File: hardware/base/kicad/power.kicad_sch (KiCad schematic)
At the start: 49 parts, among them J1 24 V, J2 USB micro-B, Q11 AO3401A, U1 TPS54360BDDAR, U2 TPD4E05U06DQAR, U3 TPS62A02ADRLR

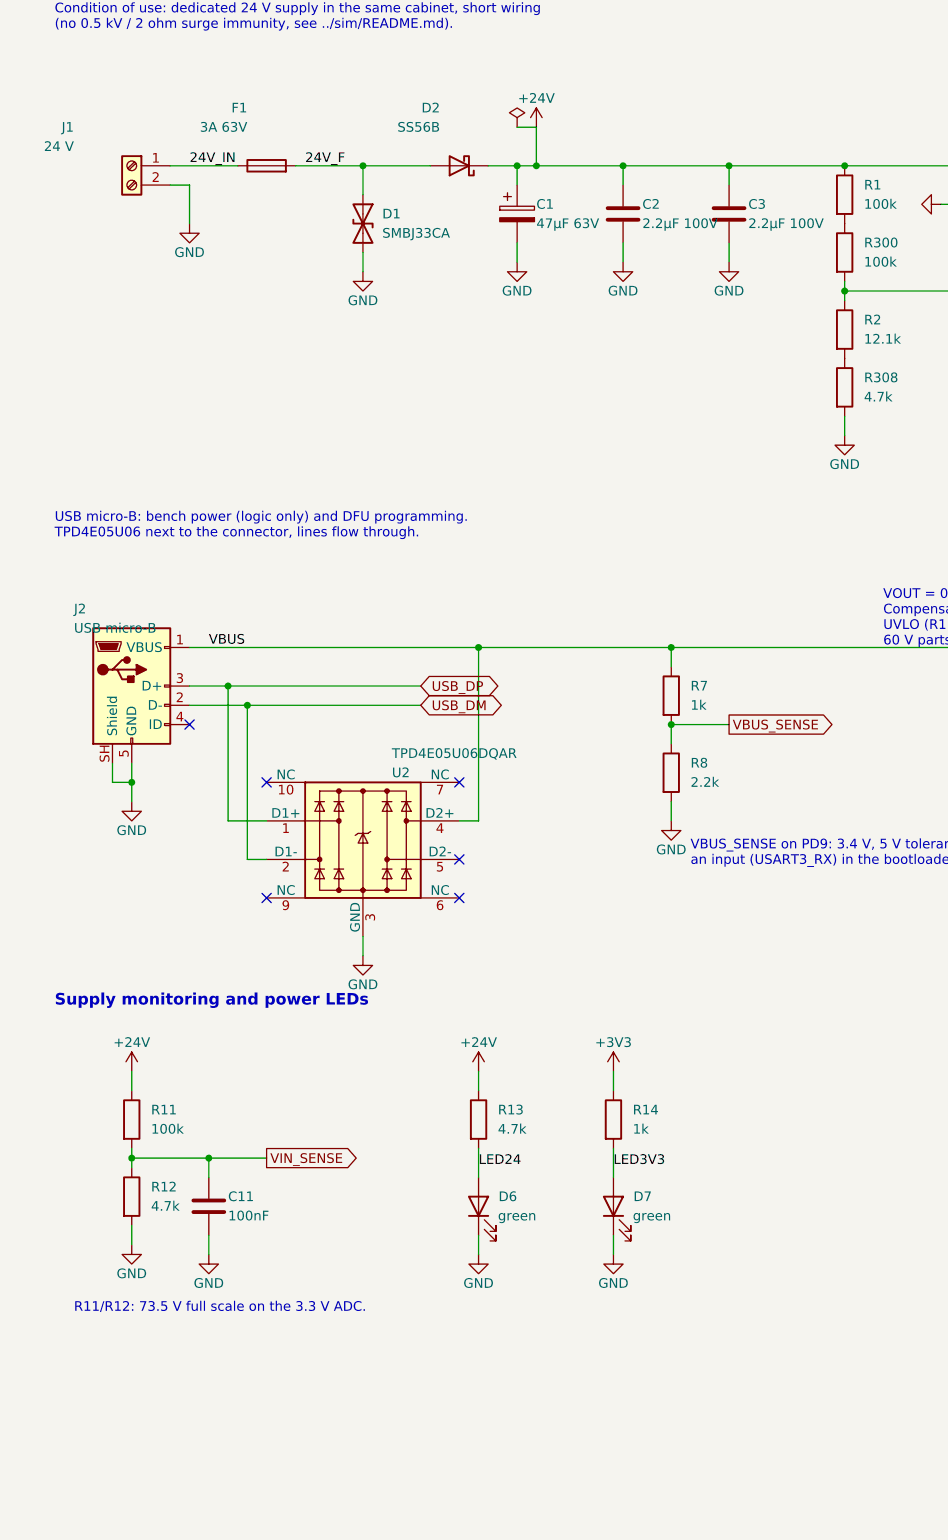
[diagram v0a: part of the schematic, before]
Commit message: Harden the base board protections and unify its terminal blocks
- TVS (SMBJ33CA) on the spindle EN and DIR drains: a relay coil driven
  without a flyback diode no longer avalanches the FET.
- ESD (5 x TPD4E05U06) on every signal of the local bus header.
- A single terminal block type, KF2EDGR-3.81-4P, five times. Pinout rule:
  pole 1 withstands 24 V, pole 2 is 0 V, so the power plug damages
  nothing whichever header it lands in.
- Functional earth on pole 3 of the power terminal block, replacing the
  M3 earth lug.
- 100 k pull-down on the DAC node: the 0-10 V output stays at 0 V while
  the DAC pin is not configured (reset, bootloader).
- "24V OUT" LED on +24V_DRV and test points on the four rails.
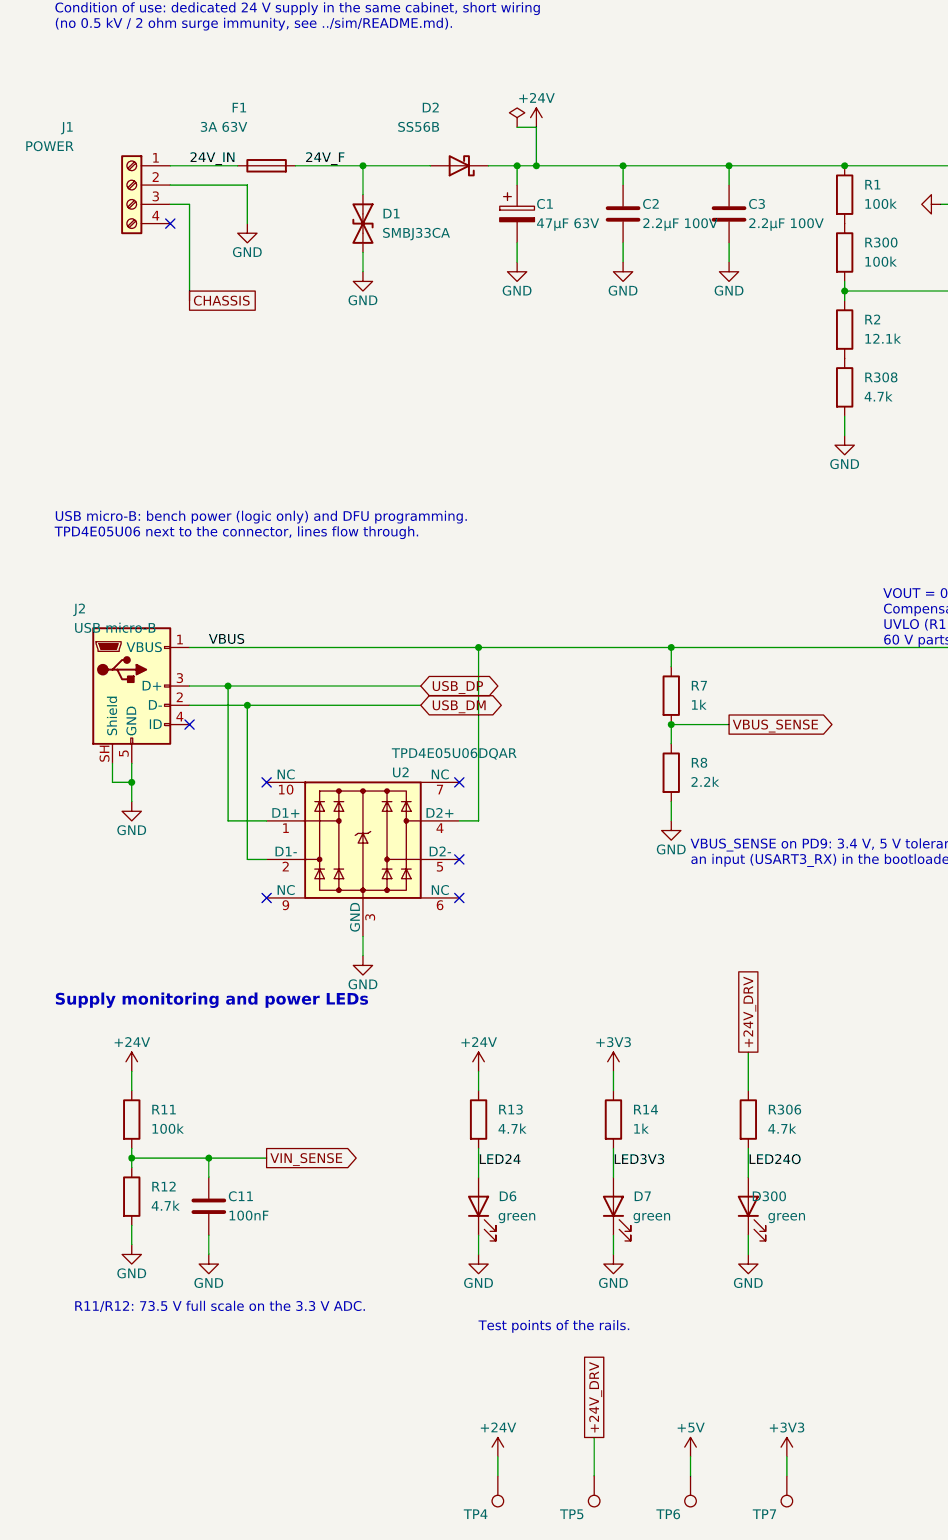
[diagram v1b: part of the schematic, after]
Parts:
- added D300: green, LED_SMD:LED_0603_1608Metric, symbol Device:LED
- added R306: 4.7k, Resistor_SMD:R_1206_3216Metric, symbol Device:R
- added TP4: +24V, TestPoint:TestPoint_Pad_D1.5mm, symbol Connector:TestPoint
- added TP5: +24V_DRV, TestPoint:TestPoint_Pad_D1.5mm, symbol Connector:TestPoint
- added TP6: +5V, TestPoint:TestPoint_Pad_D1.5mm, symbol Connector:TestPoint
- added TP7: +3V3, TestPoint:TestPoint_Pad_D1.5mm, symbol Connector:TestPoint
- J1: value 24 V -> POWER; footprint Connector_Phoenix_MSTB:PhoenixContact_MSTBA_2,5_2-G-5,08_1x02_P5.08mm_Horizontal -> Connector_Phoenix_MC:PhoenixContact_MC_1,5_4-G-3.81_1x04_P3.81mm_Horizontal; symbol Connector:Screw_Terminal_01x02 -> Connector:Screw_Terminal_01x04; LCSC C441204 -> C441184
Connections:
- net +24V: now also TP4.1
- net +3V3: now also TP7.1
- net +5V: now also TP6.1
- net GND: now also D300.1 (K)
- new net +24V_DRV: R306.1, TP5.1
- new net CHASSIS: J1.3 (Pin_3)
- new net LED24O: D300.2 (A), R306.2
- no-connect marks 7 -> 8
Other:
- note added: "Test points of the rails."

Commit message: Accept a 12 V or 24 V supply on the base board (10.8 to 30 V)
- Supply nets renamed +VIN and +VIN_OUT (silkscreen VIN OUT).
- UVLO 200 k over 47 k // 100 k: start 8.47 V (9.48 V worst case),
  stop 7.79 V; fuse 3.5 A (12H1350C).
- 0-10 V: OPA2990 rail-to-rail op amp supplied by +VIN, SS8550 current
  limit across the 120 ohm; 10 V into 10 k from 10.9 V of supply.
- E-stop and probe inputs: 2 x 4.7 k in parallel, shunts 1 k and 4.7 k.
- Buck simulated from 7.8 to 30 V with the smallest slope compensation
  the datasheet allows: 79 deg, 11.6 dB minimum.
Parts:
- F1: value 3A 63V -> 3.5A 63V; LCSC C182445 -> C182975
- R2: value 12.1k -> 47k; LCSC C25852 -> C25792
- R308: value 4.7k -> 100k; LCSC C25900 -> C25741
- TP4: value +24V -> +VIN
- TP5: value +24V_DRV -> +VIN_OUT
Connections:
- net EN: now also R308.1
- net GND: now also R2.2
- net +24V renamed +VIN
- net +24V_DRV renamed +VIN_OUT
- net 24V_F renamed VIN_F
- net 24V_IN renamed VIN_RAW
- net LED24 renamed LEDVIN
- net LED24O renamed LEDVOUT
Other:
- note added: "Logic supply VIN: 12 V or 24 V, 10.8 to 30 V (24 V: IEC 61131-2, 19.2 to 30 V). Fuse, bidirectional TVS, reverse polarity diode. Condition of use: dedicated supply in the same cabinet, short wiring (no 0.5 kV / 2 ohm surge immunity, see ../sim/README.md)."
- note added: "VOUT = 0.8 V x (1 + (R4 + R302)/(R5 + R303)) = 5.10 V, above VBUS; fsw = 658 kHz (R3 + R301 = 147 k). Compensation R6, C7 taken from the passive palette, simulated (sim/README.md). UVLO (R1 + R300 = 200 k, R2 // R308 = 32.0 k): start 8.47 V (9.48 V worst case), stop 7.79 V. 60 V parts throughout: the TVS clamps at 53.3 V."
- note removed: "24 V logic supply (IEC 61131-2: 19.2 to 30 V). Fuse, bidirectional TVS, reverse polarity diode. Condition of use: dedicated 24 V supply in the same cabinet, short wiring (no 0.5 kV / 2 ohm surge immunity, see ../sim/README.md)."
- note removed: "VOUT = 0.8 V x (1 + (R4 + R302)/(R5 + R303)) = 5.10 V, above VBUS; fsw = 658 kHz (R3 + R301 = 147 k). Compensation R6, C7 taken from the passive palette, simulated (sim/README.md). UVLO (R1 + R300 = 200 k, R2 + R308 = 16.8 k): start 15.25 V (16.97 V worst case), stop 14.57 V. 60 V parts throughout: the TVS clamps at 53.3 V."
- title: 24 V input, 5 V and 3.3 V bucks, USB -> 12 or 24 V input, 5 V and 3.3 V bucks, USB
- moved on the sheet: R308
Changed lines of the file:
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@@
 	(paper "A3")
 	(title_block
-		(title "24 V input, 5 V and 3.3 V bucks, USB")
+		(title "12 or 24 V input, 5 V and 3.3 V bucks, USB")
 		(date "2026-10-18")
 		(rev "A")

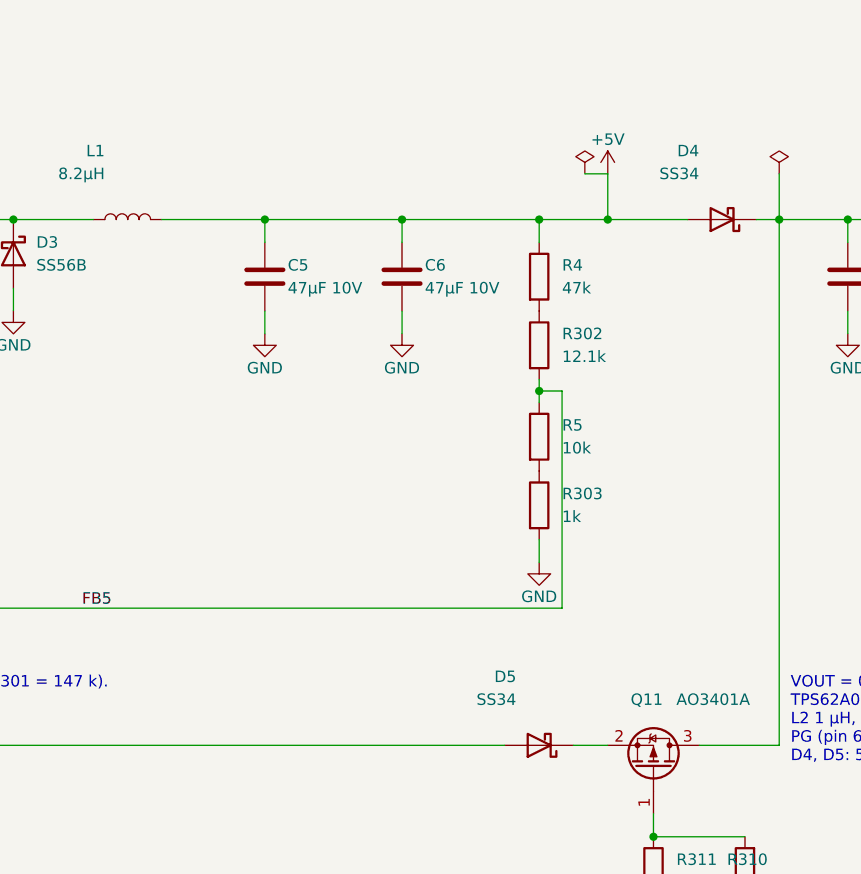
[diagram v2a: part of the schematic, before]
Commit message: Trim the base board BOM: 60 to 58 lines
- ESD of NRST and of the PWM output on one channel of the TPD4E05U06
  already used on the PHY lines, instead of a PESD5V0S1BA.
- SS56B instead of SS34 for the 5 V / USB OR-ing and the encoder
  supplies.
- One 100 uF 10 V X5R 1210 on the 5 V buck output instead of two 47 uF:
  about 55 uF at 5 V, inside the simulated 34-80 uF.
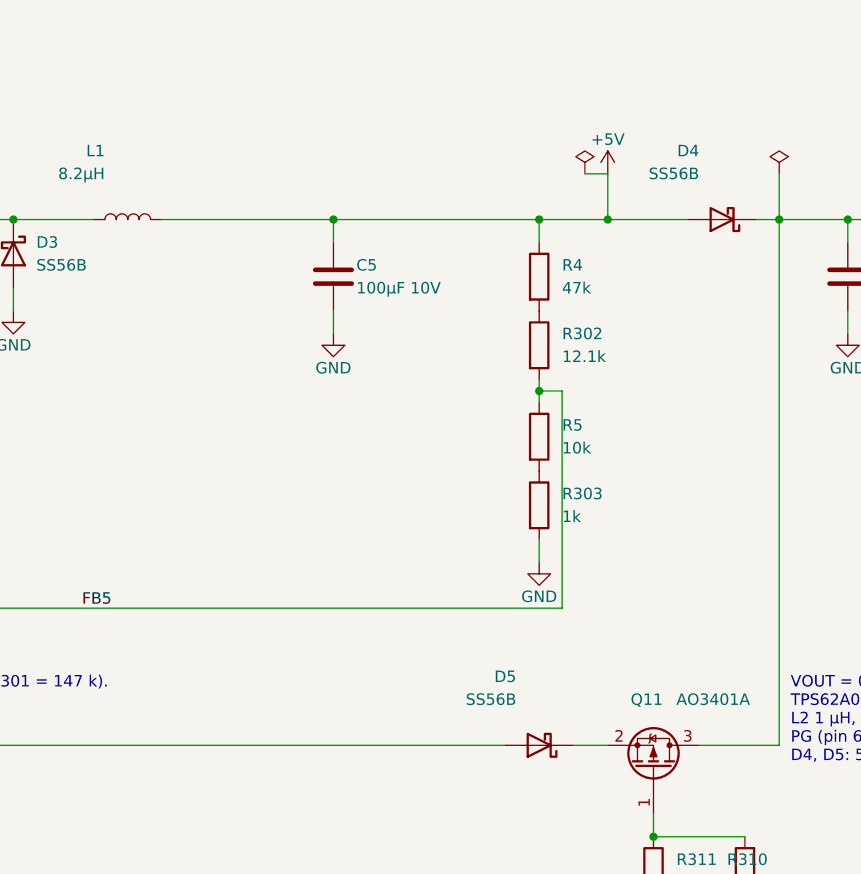
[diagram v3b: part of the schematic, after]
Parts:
- removed C6: 47µF 10V, Capacitor_SMD:C_1210_3225Metric, symbol Device:C
- C5: value 47µF 10V -> 100µF 10V; LCSC C84494 -> C84455
- D4, D5: value SS34 -> SS56B; footprint Diode_SMD:D_SMA -> Diode_SMD:D_SMB; LCSC C8678 -> C14651
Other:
- moved on the sheet: C5

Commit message: Widen the base board to 107.5 x 150 mm, vertical USB, PE contact hole
- The parts covered 94 % of the free top area on 72 mm, 53 % on 107.5 mm:
  Phoenix UM-BASIC 108 profile (kit UM-BASIC-KIT-B108-L150-7035), one side.
- M3 holes at the four corners; H1 plated next to POWER.
- H5: plated hole for the Phoenix PE contact L1, which earths CHASSIS to
  the DIN rail; no lead over the contact body under the board.
- USB jack: vertical Molex 105133-0001, to sit next to the MCU.
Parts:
- J2: footprint Connector_USB:USB_Micro-B_Amphenol_10118194-0001LF_Horizontal -> Connector_USB:USB_Micro-B_Molex-105133-0001; LCSC C132563 -> C782257

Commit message: Place the base board parts; DIP switches for the encoder terminations
Placement (gen/pcb.py): one zone per schematic sheet, key parts placed by
hand, the other parts next to the pin they serve, bulkiest first, with a
1 mm gap preferred when it costs at most 2 mm. The local bus header stands
at the left end, centred across the board, facing the modules.

Encoder terminations: one CTS 218-4LPSTR DIP switch per encoder (100 mA
non-switching) replaces three SMD jumpers; the supply selector and the
Modbus termination use a through-hole 1x3 header. Split DIP symbol, one
unit per switch, drawn on the pair it serves.

DRC rules: 0.2 mm thermal vias, per-package clearance for 0.65 mm pitch
parts. Test points out of the BOM, DNP copied to the footprints. pcb.py
keeps the schematic settings of the project file and finds the KiCad
footprint libraries on every install.

Claude-Session: https://claude.ai/code/session_01JfmMsHNpEd1mfzHNWc4koJ
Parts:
- TP4, TP5, TP6, TP7: now left out of the parts list

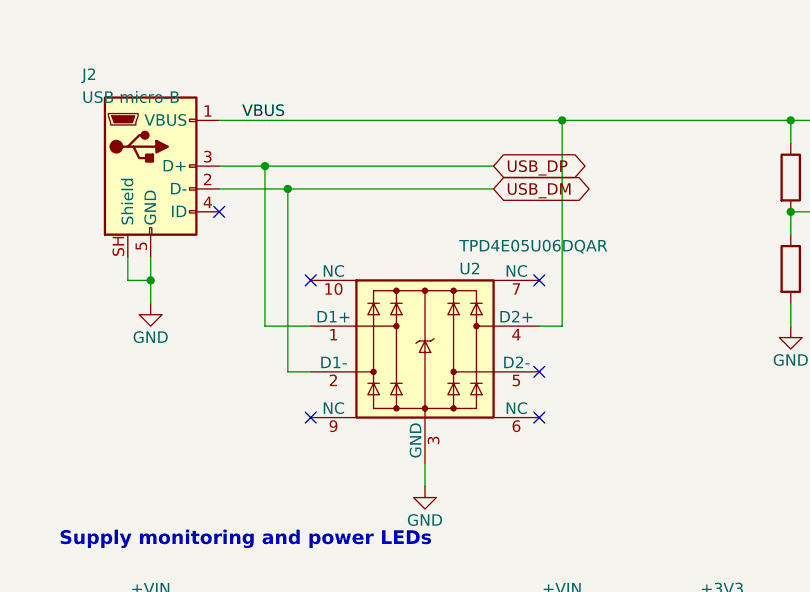
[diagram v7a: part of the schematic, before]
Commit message: Differential pairs routed by script; PHY to jack mapping for a planar layout
- pairs.py, pass "pairs" right after the planes and trunks: A* on a 0.1 mm
  grid for the centre line of each pair, clear of the other copper by about
  3 W (by the clearance alone near the pads), offset into its two lines;
  straight out of the QFN pads, straight through the ESD arrays, each line on
  its own into the through-hole pins of the jack. Ethernet 100 ohm and USB
  90 ohm at 0.15 mm gap (sim/impedance.py).
- Schematic: the lines on the jack pins and ESD channels in the order that
  routes without a crossing (port A with P and N swapped, port B with TX and
  RX swapped: the LAN9253 PHYs correct the polarity and have HP Auto-MDIX);
  the NC pins of the ESD arrays opposite each line carry it (TI flow-through).
- Ethernet terminations lifted off the board while the pairs are routed, then
  put against their line, 2 to 10 mm from the PHY pins; the lines inside a
  port straddled by their 0603 termination (49.9 ohm moved to 0603, C23185,
  basic, 1.78 M in stock on 2026-10-20; clock series resistors too).
- Placement: lanes of the pairs kept free of other parts (LAN9253 checklist);
  ESD arrays in the way of their lines; centre tap capacitors at the jacks;
  VDD33TXRX mini-planes in layer 3 under the terminations.
- route.py: real C-LOCK cutout clearance for copper; via hole to pad
  clearance; mini-plane priority in the plane test.
- kicadgen: tagged labels do not name a net (a second label on a NC pin).

Claude-Session: https://claude.ai/code/session_01D6Na26JP4CWdxCU6BKa4Yc
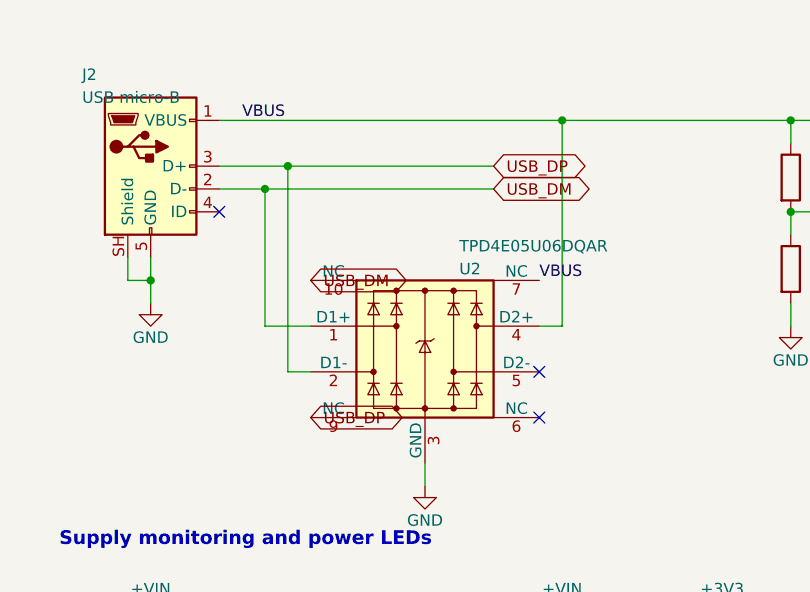
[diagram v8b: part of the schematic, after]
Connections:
- net USB_DM: now also U2.1 (D1+), U2.10 (NC); no longer U2.2 (D1-)
- net USB_DP: now also U2.2 (D1-), U2.9 (NC); no longer U2.1 (D1+)
- net VBUS: now also U2.7 (NC)
- no-connect marks 8 -> 5
